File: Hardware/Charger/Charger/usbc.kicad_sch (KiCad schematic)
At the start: 4 parts, among them J401 USB_C_Receptacle_USB2.0_16P, U401 USBLC6-2SC6

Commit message: built charger schematic and added parts to layout
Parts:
- R401, R402: footprint footprints:R_0603_1608Metric -> Resistor_SMD:R_0603_1608Metric
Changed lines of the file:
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@@
 			)
 		)
-		(property "Footprint" "footprints:R_0603_1608Metric"
+		(property "Footprint" "Resistor_SMD:R_0603_1608Metric"
 			(at 139.7 90.678 90)
 			(effects
@@
 			)
 		)
-		(property "Footprint" "footprints:R_0603_1608Metric"
+		(property "Footprint" "Resistor_SMD:R_0603_1608Metric"
 			(at 139.7 93.218 90)
 			(effects

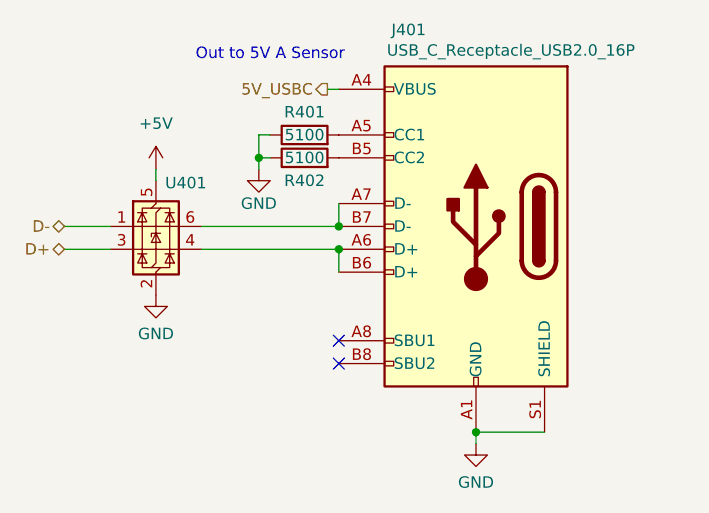
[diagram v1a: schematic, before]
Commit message: Completed PCB layout of charger
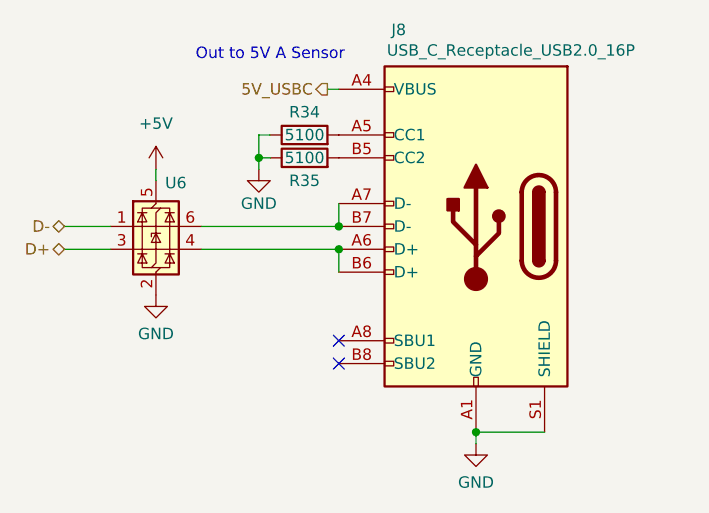
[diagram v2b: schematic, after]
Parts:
- renumbered J401 to J8, R401 to R34, R402 to R35, U401 to U6
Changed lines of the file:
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@@
 		(on_board yes)
 		(dnp no)
-		(property "Reference" "#PWR0403"
+		(property "Reference" "#PWR078"
 			(at 134.62 99.06 0)
 			(effects
@@
 			(project "Charger"
 				(path "/ec0cb266-3da5-4155-a0e5-38a3c68d3210/94dc2c9c-6360-4f0e-81c0-d08593c9f773/dc9c6c82-2ca0-4595-949b-0b07300fa078"
-					(reference "#PWR0403")
+					(reference "#PWR078")
 					(unit 1)
 				)
@@
 		(on_board yes)
 		(dnp no)
-		(property "Reference" "U401"
+		(property "Reference" "U6"
 			(at 124.206 94.234 0)
 			(effects
@@
 			(project "Charger"
 				(path "/ec0cb266-3da5-4155-a0e5-38a3c68d3210/94dc2c9c-6360-4f0e-81c0-d08593c9f773/dc9c6c82-2ca0-4595-949b-0b07300fa078"
-					(reference "U401")
+					(reference "U6")
 					(unit 1)
 				)
@@
 		(on_board yes)
 		(dnp no)
-		(property "Reference" "#PWR0404"
+		(property "Reference" "#PWR079"
 			(at 158.75 129.54 0)
 			(effects
@@
 			(project "Charger"
 				(path "/ec0cb266-3da5-4155-a0e5-38a3c68d3210/94dc2c9c-6360-4f0e-81c0-d08593c9f773/dc9c6c82-2ca0-4595-949b-0b07300fa078"
-					(reference "#PWR0404")
+					(reference "#PWR079")
 					(unit 1)
 				)
@@
 		(on_board yes)
 		(dnp no)
-		(property "Reference" "J401"
+		(property "Reference" "J8"
 			(at 149.352 77.216 0)
 			(effects
@@
 			(project "Charger"
 				(path "/ec0cb266-3da5-4155-a0e5-38a3c68d3210/94dc2c9c-6360-4f0e-81c0-d08593c9f773/dc9c6c82-2ca0-4595-949b-0b07300fa078"
-					(reference "J401")
+					(reference "J8")
 					(unit 1)
 				)
@@
 		(dnp no)
 		(fields_autoplaced yes)
-		(property "Reference" "#PWR0401"
+		(property "Reference" "#PWR076"
 			(at 123.19 96.52 0)
 			(effects
@@
 			(project "Charger"
 				(path "/ec0cb266-3da5-4155-a0e5-38a3c68d3210/94dc2c9c-6360-4f0e-81c0-d08593c9f773/dc9c6c82-2ca0-4595-949b-0b07300fa078"
-					(reference "#PWR0401")
+					(reference "#PWR076")
 					(unit 1)
 				)
@@
 		(on_board yes)
 		(dnp no)
-		(property "Reference" "R401"
+		(property "Reference" "R34"
 			(at 139.7 86.36 90)
 			(effects
@@
 			(project "Charger"
 				(path "/ec0cb266-3da5-4155-a0e5-38a3c68d3210/94dc2c9c-6360-4f0e-81c0-d08593c9f773/dc9c6c82-2ca0-4595-949b-0b07300fa078"
-					(reference "R401")
+					(reference "R34")
 					(unit 1)
 				)
@@
 		(on_board yes)
 		(dnp no)
-		(property "Reference" "R402"
+		(property "Reference" "R35"
 			(at 139.7 93.98 90)
 			(effects
@@
 			(project "Charger"
 				(path "/ec0cb266-3da5-4155-a0e5-38a3c68d3210/94dc2c9c-6360-4f0e-81c0-d08593c9f773/dc9c6c82-2ca0-4595-949b-0b07300fa078"
-					(reference "R402")
+					(reference "R35")
 					(unit 1)
 				)
@@
 		(on_board yes)
 		(dnp no)
-		(property "Reference" "#PWR0402"
+		(property "Reference" "#PWR077"
 			(at 123.19 113.03 0)
 			(effects
@@
 			(project "Charger"
 				(path "/ec0cb266-3da5-4155-a0e5-38a3c68d3210/94dc2c9c-6360-4f0e-81c0-d08593c9f773/dc9c6c82-2ca0-4595-949b-0b07300fa078"
-					(reference "#PWR0402")
-					(unit 1)
-				)
+					(reference "#PWR077")
+					(unit 1)
+				)
